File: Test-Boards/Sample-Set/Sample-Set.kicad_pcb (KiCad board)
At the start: 2 copper layers, 1 part

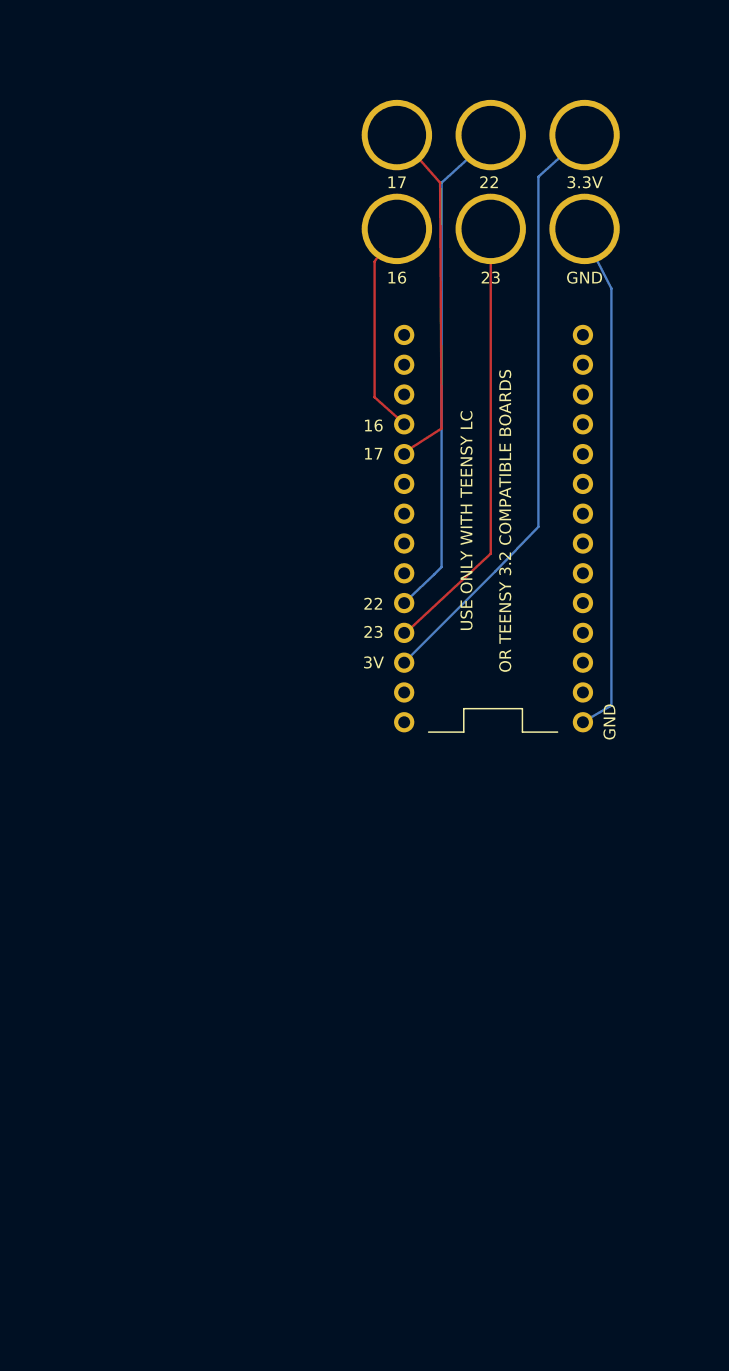
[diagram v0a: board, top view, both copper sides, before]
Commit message: Sample set ordered. More minor lib tweaks.
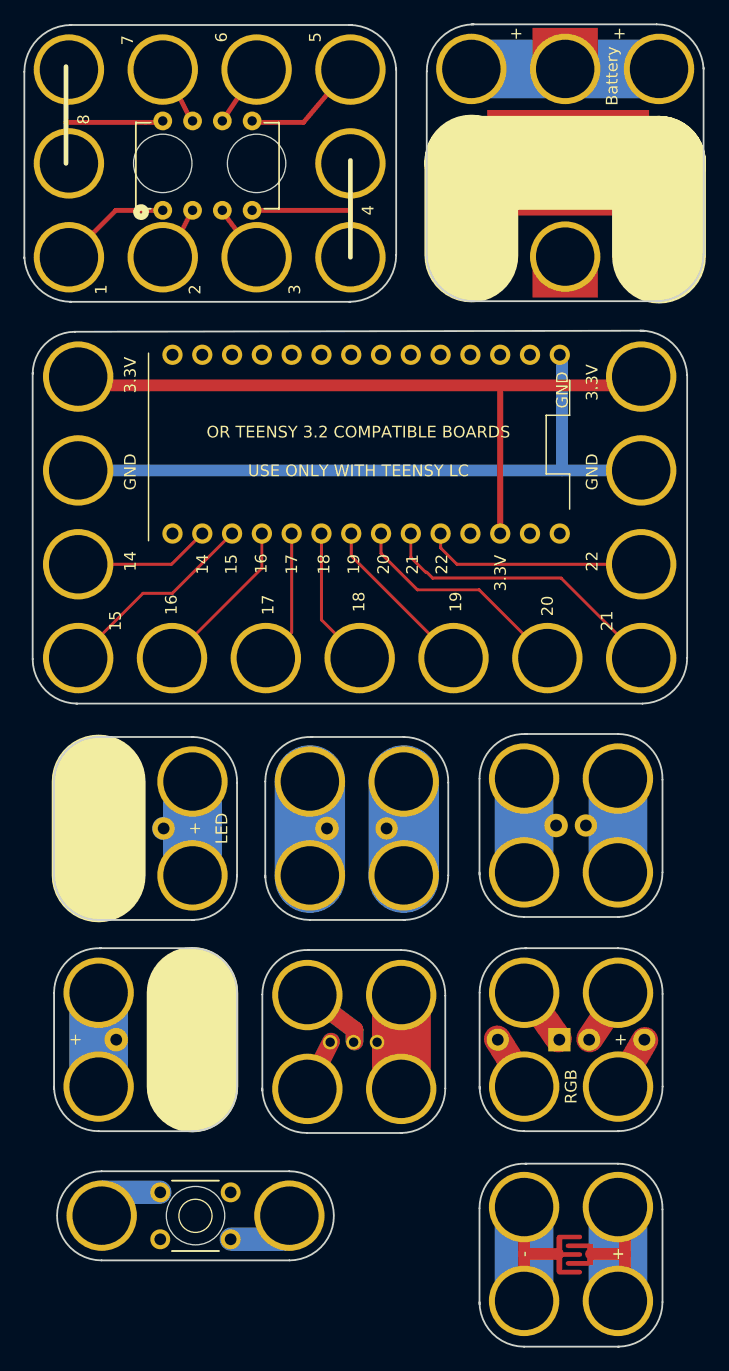
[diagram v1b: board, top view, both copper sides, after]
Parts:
- removed the REF** at (94.0, 81.0)
- added 3POS SWITCH: SLIDE, Rewire_Circuits:SWITCH-SPDT-3PIN-2.5mmPITCH-TH-2x2, F.Cu at (94.4, 154.3)
- added BT1: Battery, Rewire_Circuits:CR2032-3x3-NO-ROTATE, F.Cu at (116.3, 83.4)
- added DIP8 BREAKOUT: 8DIP IC, Rewire_Circuits:DIP8-PLATFORM-TEST, F.Cu at (90.0, 83.4)
- added GEN 2.54MM PITCH: GENERIC-TH-2.54MM-PITCH, Rewire_Circuits:GENERIC-2.54MM-TH-2x2, F.Cu at (112.8, 135.9)
- added GEN 5MM PITCH: GENERIC-TH-5MM, Rewire_Circuits:GENERIC-5MM-TH-2x2, F.Cu at (94.6, 136.1)
- added LED: Val**, Rewire_Circuits:LED-10MMD-5MMP-TH-2x2, F.Cu at (76.6, 154.1)
- added LED 2.54MM PITCH: LED, Rewire_Circuits:LED-5MMD-2.5MMP-2x2, F.Cu at (76.6, 136.1)
- added PUSHBUTTON: Pushbutton, Rewire_Circuits:BUTTON-1x3-TH-OMRON-B3F-1XXX, F.Cu at (68.8, 165.1)
- added REF**: DIP-8_W7.62mm, Rewire_Circuits:TEENSYLC-EDGE-4x7, F.Cu at (66.8, 117.6)
- added RGB LED: RGB, Rewire_Circuits:LED-RGB-5MMD-2.5MMP-2x2, F.Cu at (112.8, 154.1)
- added TOUCH: TOUCH, Rewire_Circuits:TOUCH-SMT-2x2, F.Cu at (112.8, 172.4)
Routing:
- net (no net): track 0.00 -> 157.1 mm
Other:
- board outline added: 57.9 x 112.7 mm
- board text added: "Sample Set Information Rewire Circuits 11/20/16"
